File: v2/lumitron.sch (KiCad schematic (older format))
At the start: 11 parts

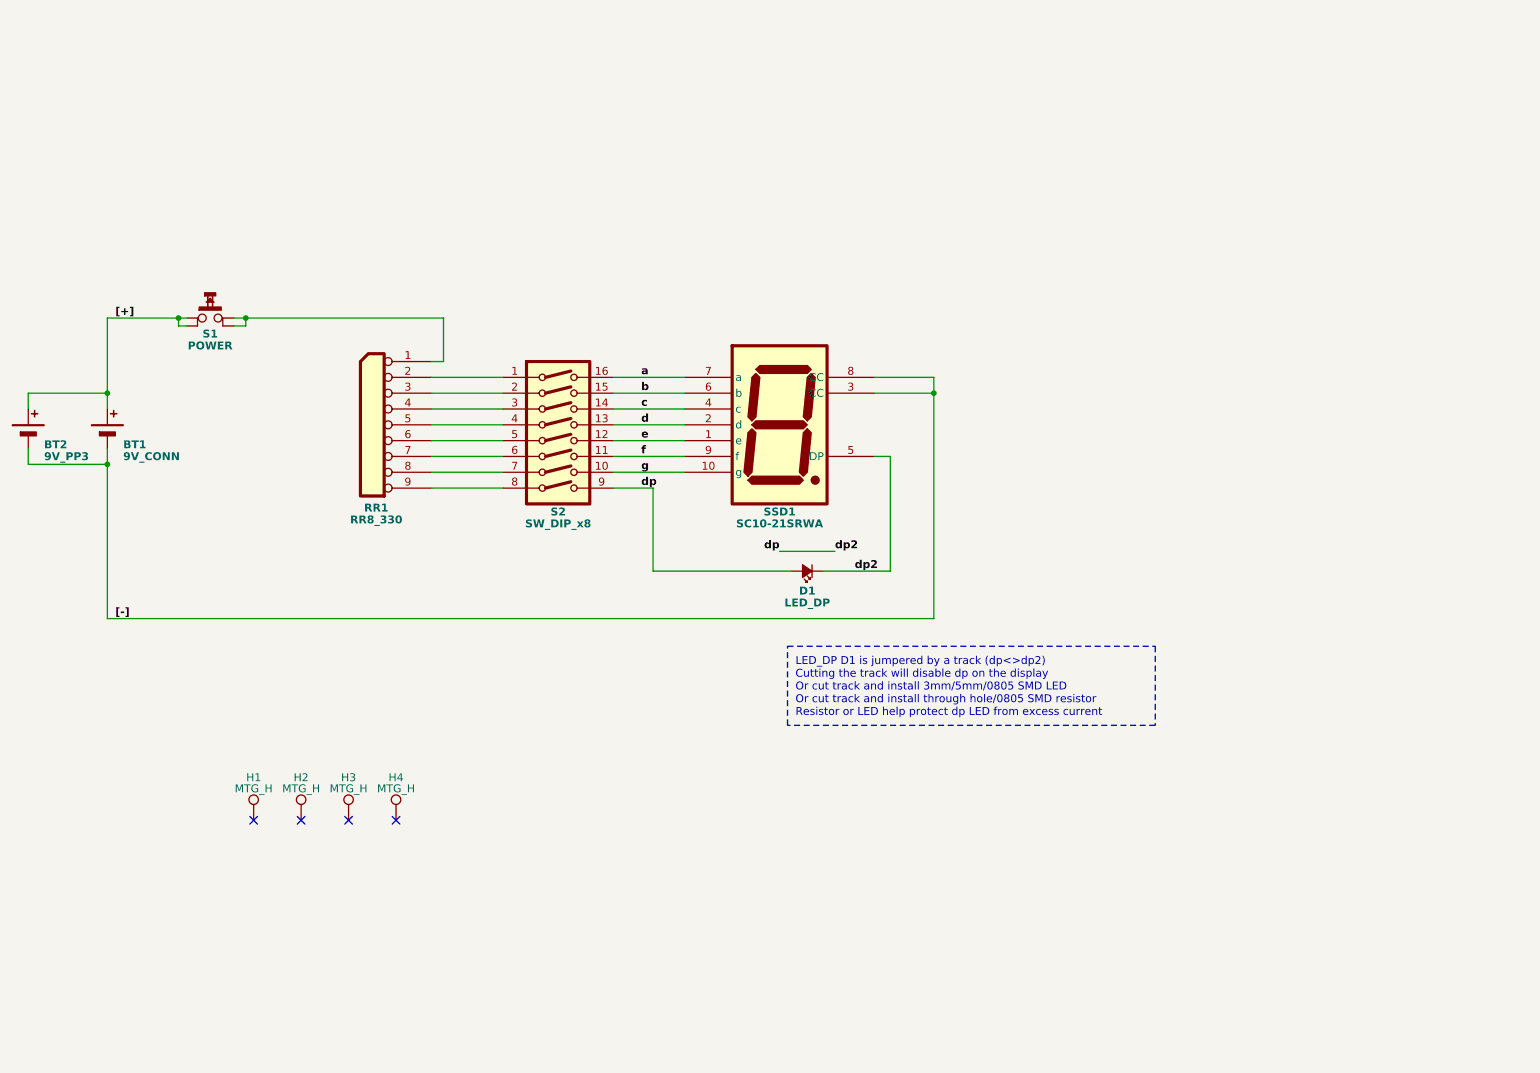
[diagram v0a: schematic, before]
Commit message: added open source logo
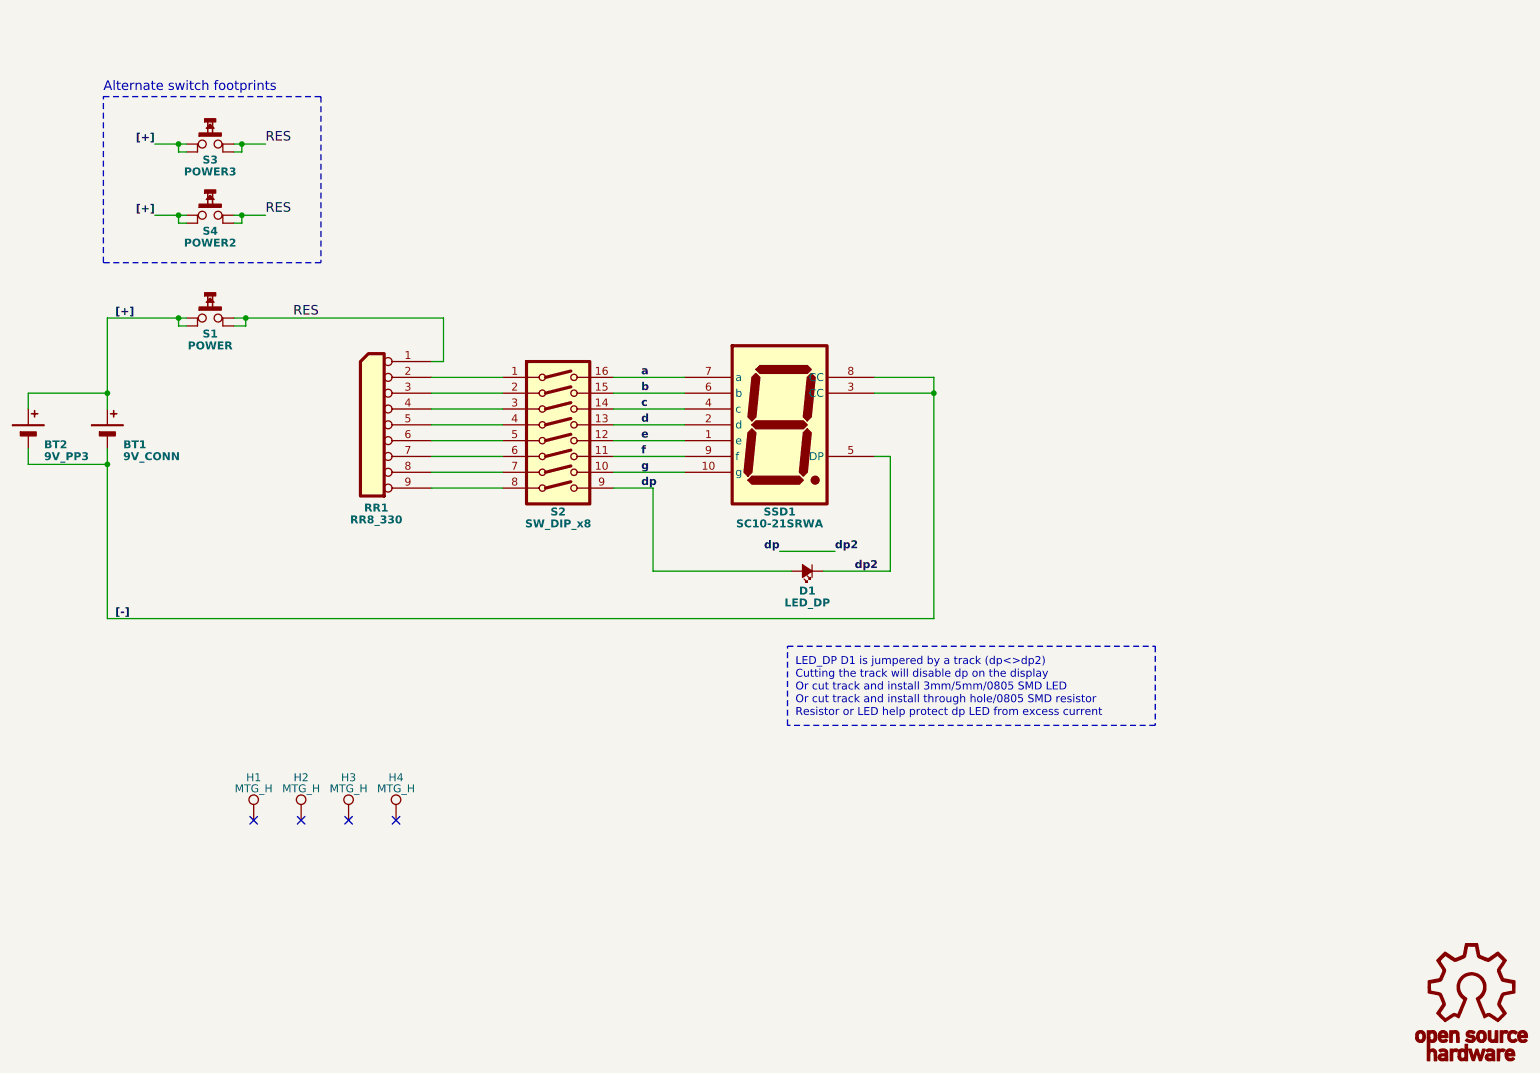
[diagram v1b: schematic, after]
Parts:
- added G1: OSHW, lumitron_pcb:OSHW_6mm, symbol OSHW
- added S3: POWER3, lumitron_pcb:sw_KSA_Tactile_SPST, symbol SPST-M
- added S4: POWER2, lumitron_pcb:sw_KS-01Q, symbol SPST-M
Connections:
- net [+]: now also S3.1, S3.3, S4.1, S4.3
- net RES: now reaches RR1.1 (COM), S1.2, S1.4
- net RES: now also S3.2, S3.4, S4.2, S4.4
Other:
- note added: "Alternate switch footprints"
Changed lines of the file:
@@
 LIBS:contrib
 LIBS:valves
+LIBS:RAF-cache
 LIBS:lumitron-cache
 EELAYER 25 0
@@
 Wire Notes Line
 	6475 5225 6475 4725
+$Comp
+L SPST-M S4
+U 1 1 59BE6274
+P 2825 2000
+F 0 "S4" H 2825 1900 50  0000 C CNB
+F 1 "POWER2" H 2825 1825 50  0000 C CNB
+F 2 "lumitron_pcb:sw_KS-01Q" H 2825 2000 60  0001 C CNN
+F 3 "" H 2825 2000 60  0000 C CNN
+	1    2825 2000
+	1    0    0    -1
+$EndComp
+$Comp
+L SPST-M S3
+U 1 1 59BE62D4
+P 2825 1550
+F 0 "S3" H 2825 1450 50  0000 C CNB
+F 1 "POWER3" H 2825 1375 50  0000 C CNB
+F 2 "lumitron_pcb:sw_KSA_Tactile_SPST" H 2825 1550 60  0001 C CNN
+F 3 "" H 2825 1550 60  0000 C CNN
+	1    2825 1550
+	1    0    0    -1
+$EndComp
+Text Label 3350 2650 0    60   ~ 0
+RES
+Wire Wire Line
+	2675 2050 2625 2050
+Wire Wire Line
+	2625 2050 2625 2000
+Wire Wire Line
+	2475 2000 2675 2000
+Wire Wire Line
+	2975 2050 3025 2050
+Wire Wire Line
+	3025 2050 3025 2000
+Wire Wire Line
+	2975 2000 3175 2000
+Wire Wire Line
+	2675 1600 2625 1600
+Wire Wire Line
+	2625 1600 2625 1550
+Wire Wire Line
+	2475 1550 2675 1550
+Wire Wire Line
+	2975 1600 3025 1600
+Wire Wire Line
+	3025 1600 3025 1550
+Wire Wire Line
+	2975 1550 3175 1550
+Connection ~ 2625 1550
+Connection ~ 2625 2000
+Connection ~ 3025 1550
+Connection ~ 3025 2000
+Text Label 2475 2000 2    50   ~ 10
+[+]
+Text Label 2475 1550 2    50   ~ 10
+[+]
+Text Label 3175 2000 0    60   ~ 0
+RES
+Text Label 3175 1550 0    60   ~ 0
+RES
+Wire Notes Line
+	2150 1250 3525 1250
+Wire Notes Line
+	3525 1250 3525 2300
+Wire Notes Line
+	3525 2300 2150 2300
+Wire Notes Line
+	2150 2300 2150 1250
+Text Notes 2150 1225 0    60   ~ 0
+Alternate switch footprints
+$Comp
+L OSHW G1
+U 1 1 59BE6DD5
+P 10800 6975
+F 0 "G1" H 10800 6925 40  0001 C CNN
+F 1 "OSHW" H 10800 7075 40  0001 C CNN
+F 2 "lumitron_pcb:OSHW_6mm" H 10800 6975 60  0001 C CNN
+F 3 "" H 10800 6975 60  0000 C CNN
+F 4 "mfr_pn" H 10800 6975 60  0001 C CNN "manf#"
+	1    10800 6975
+	1    0    0    -1
+$EndComp
 $EndSCHEMATC

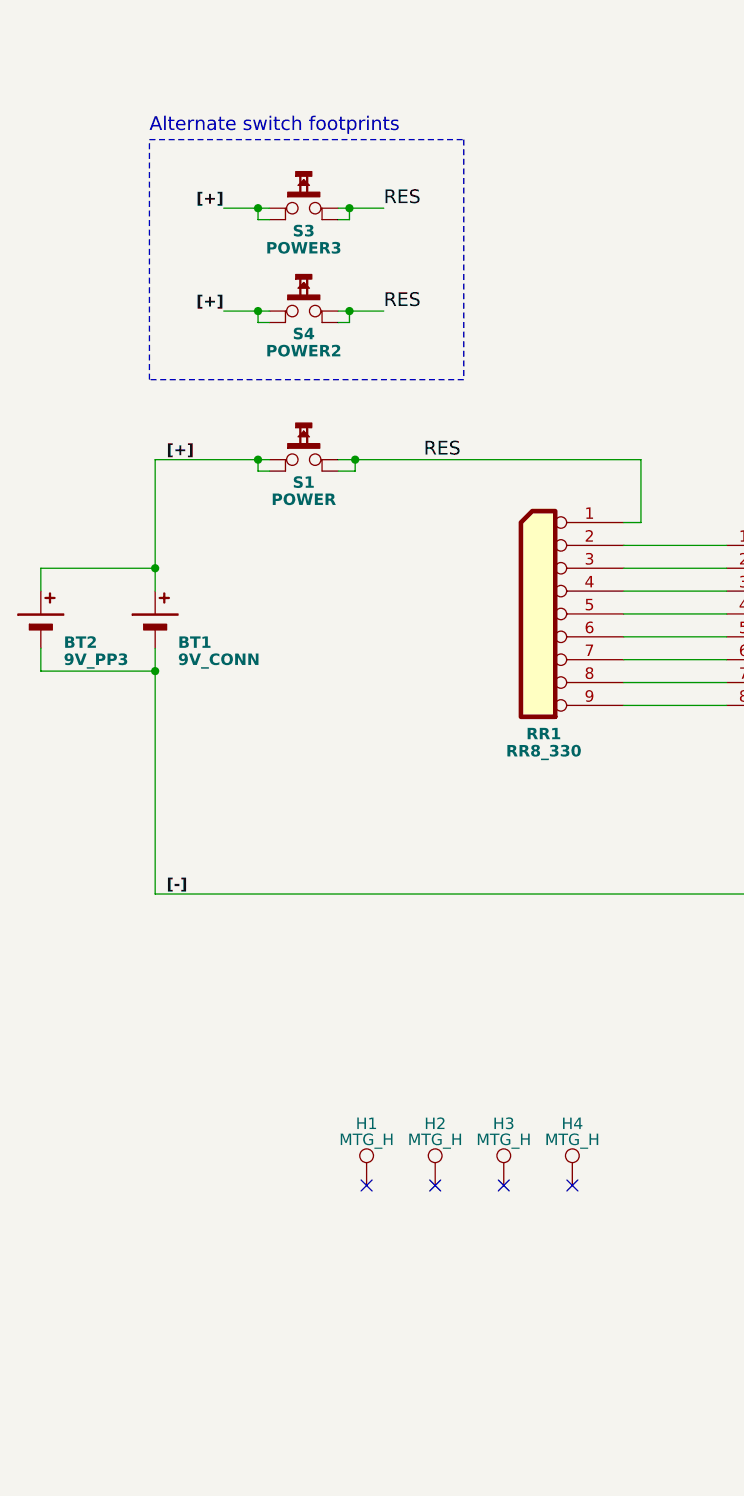
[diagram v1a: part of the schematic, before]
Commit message: added Power momentary push button
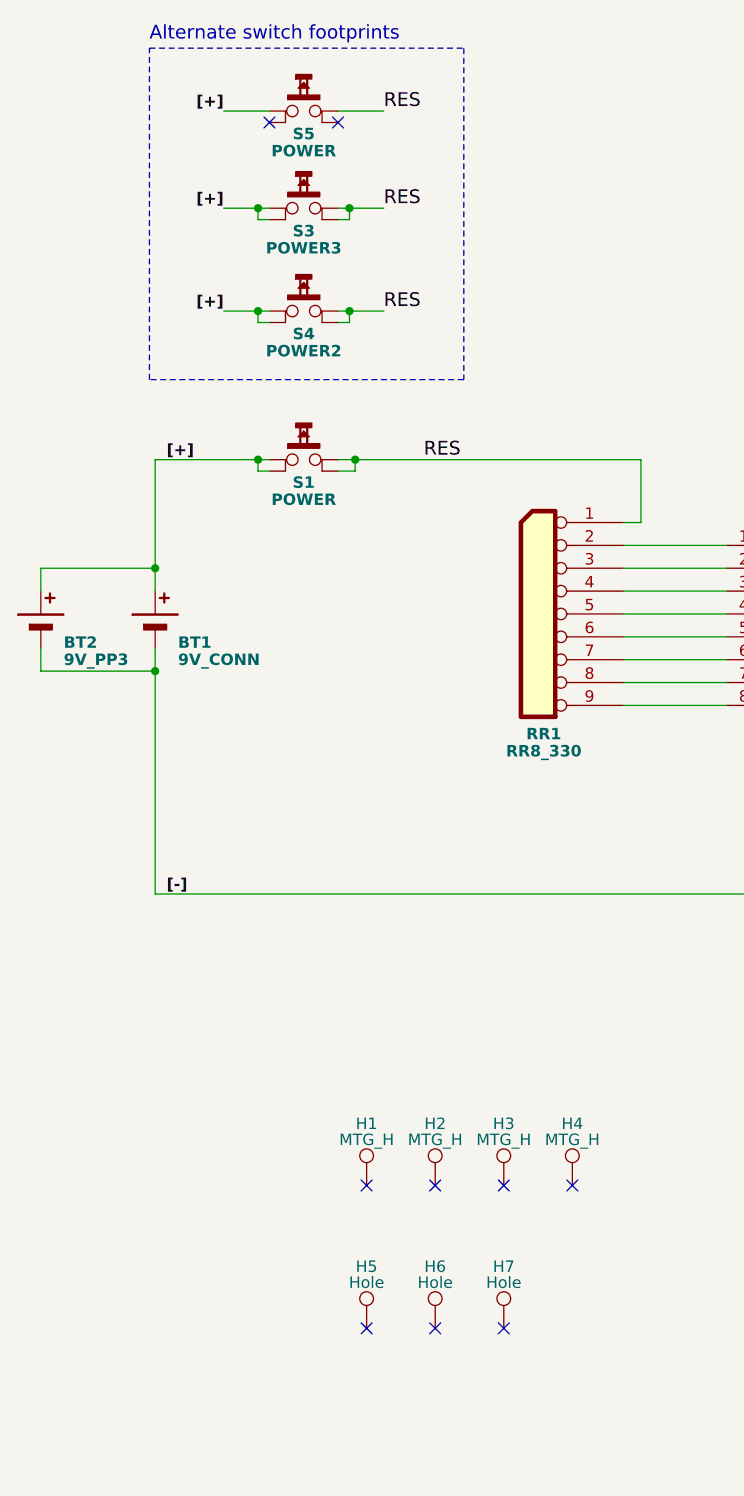
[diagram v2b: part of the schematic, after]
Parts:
- added H5, H6, H7: Hole, lumitron_pcb:MountingHole_3-7mm, symbol TEST_1P
- added S5: POWER, lumitron_pcb:switch_MJTP1250, symbol SPST-M
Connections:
- net RES: now also S5.2
- net [+]: now also S5.1
- no-connect marks 4 -> 9
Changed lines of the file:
@@
 LIBS:contrib
 LIBS:valves
-LIBS:RAF-cache
 LIBS:lumitron-cache
 EELAYER 25 0
@@
 RES
 Wire Notes Line
-	2150 1250 3525 1250
-Wire Notes Line
-	3525 1250 3525 2300
+	2150 850  3525 850
 Wire Notes Line
 	3525 2300 2150 2300
-Wire Notes Line
-	2150 2300 2150 1250
-Text Notes 2150 1225 0    60   ~ 0
+Text Notes 2150 825  0    60   ~ 0
 Alternate switch footprints
 $Comp
@@
 	1    0    0    -1
 $EndComp
+$Comp
+L TEST_1P H5
+U 1 1 59C947AF
+P 3100 6450
+F 0 "H5" H 3100 6720 50  0000 C CNN
+F 1 "Hole" H 3100 6650 50  0000 C CNN
+F 2 "lumitron_pcb:MountingHole_3-7mm" H 3300 6450 50  0001 C CNN
+F 3 "" H 3300 6450 50  0000 C CNN
+	1    3100 6450
+	1    0    0    -1
+$EndComp
+$Comp
+L TEST_1P H6
+U 1 1 59C947B5
+P 3400 6450
+F 0 "H6" H 3400 6720 50  0000 C CNN
+F 1 "Hole" H 3400 6650 50  0000 C CNN
+F 2 "lumitron_pcb:MountingHole_3-7mm" H 3600 6450 50  0001 C CNN
+F 3 "" H 3600 6450 50  0000 C CNN
+	1    3400 6450
+	1    0    0    -1
+$EndComp
+$Comp
+L TEST_1P H7
+U 1 1 59C947BB
+P 3700 6450
+F 0 "H7" H 3700 6720 50  0000 C CNN
+F 1 "Hole" H 3700 6650 50  0000 C CNN
+F 2 "lumitron_pcb:MountingHole_3-7mm" H 3900 6450 50  0001 C CNN
+F 3 "" H 3900 6450 50  0000 C CNN
+	1    3700 6450
+	1    0    0    -1
+$EndComp
+NoConn ~ 3100 6450
+NoConn ~ 3400 6450
+NoConn ~ 3700 6450
+$Comp
+L SPST-M S5
+U 1 1 59C94A2D
+P 2825 1125
+F 0 "S5" H 2825 1025 50  0000 C CNB
+F 1 "POWER" H 2825 950 50  0000 C CNB
+F 2 "lumitron_pcb:switch_MJTP1250" H 2825 1125 60  0001 C CNN
+F 3 "" H 2825 1125 60  0000 C CNN
+	1    2825 1125
+	1    0    0    -1
+$EndComp
+Wire Wire Line
+	2475 1125 2675 1125
+Wire Wire Line
+	2975 1125 3175 1125
+Text Label 2475 1125 2    50   ~ 10
+[+]
+Text Label 3175 1125 0    60   ~ 0
+RES
+NoConn ~ 2975 1175
+NoConn ~ 2675 1175
+Wire Notes Line
+	2150 2300 2150 850
+Wire Notes Line
+	3525 850  3525 2300
 $EndSCHEMATC
